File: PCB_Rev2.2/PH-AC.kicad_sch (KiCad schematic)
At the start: 52 parts, among them J1 USB_C_Receptacle_USB2.0_14P, J2 Conn_01x03, Q1 DMG1012T, SW1 SW_Push, U1 RP2040, U2 RT6150B-33GQW, U3 W25Q16JVSS, Y1 Crystal_GND24

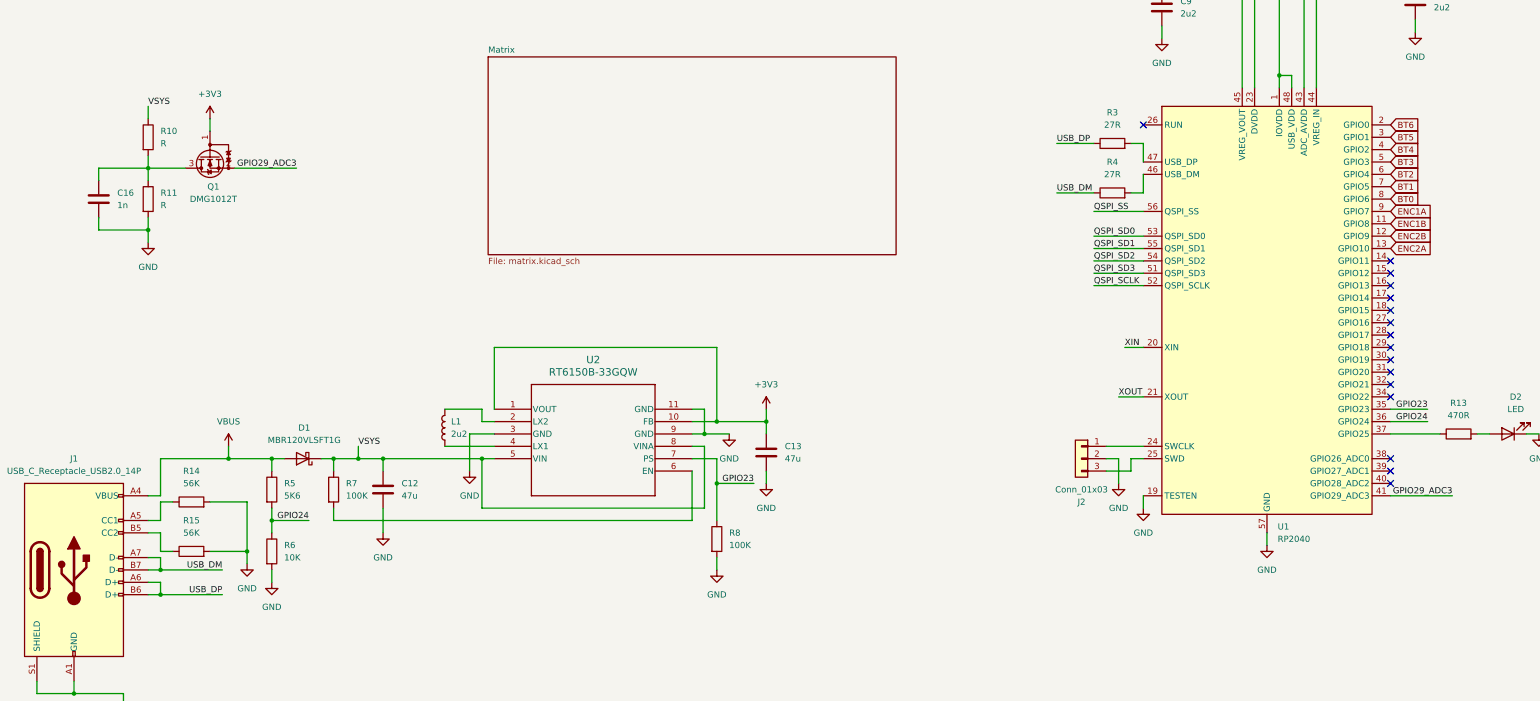
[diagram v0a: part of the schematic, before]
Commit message: LDO Modification
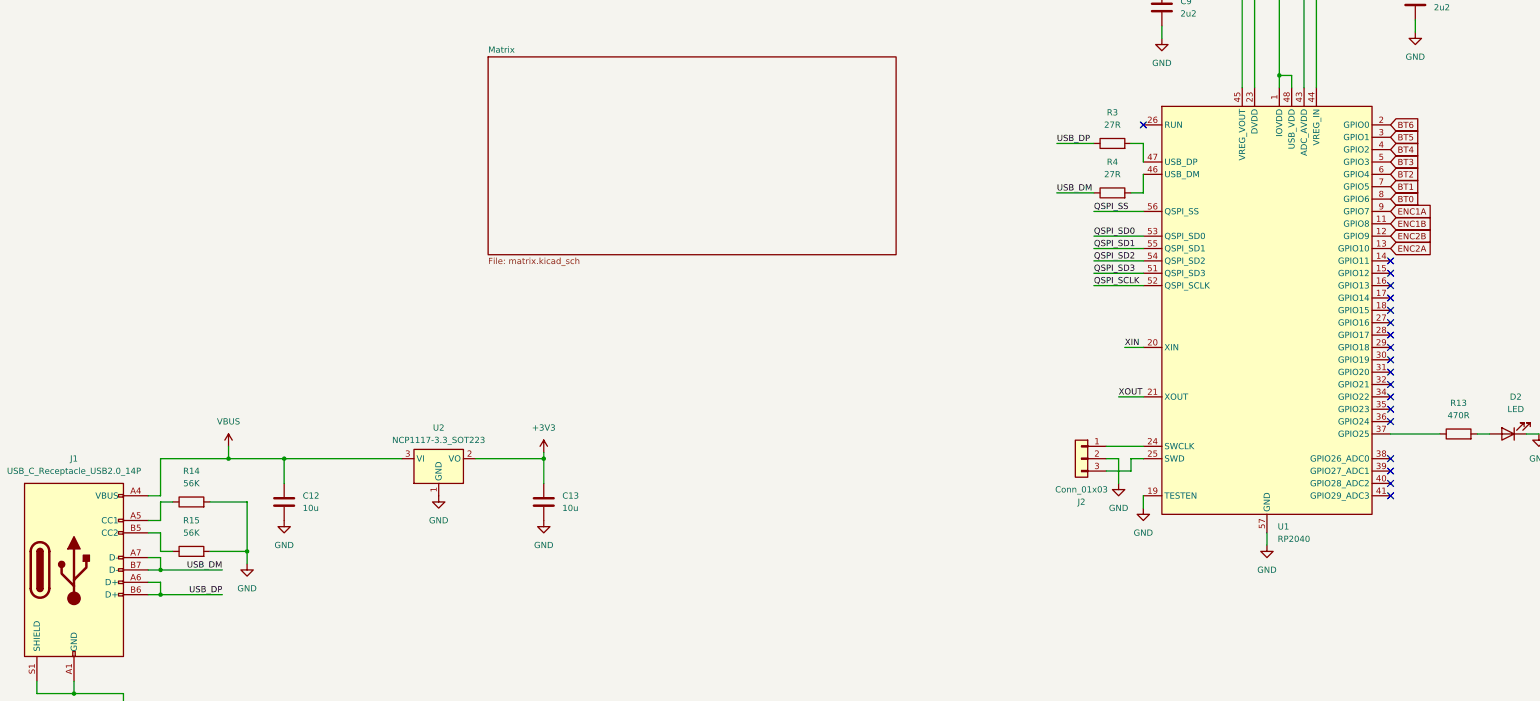
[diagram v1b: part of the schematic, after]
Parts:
- removed C16: 1n, Capacitor_SMD:C_0402_1005Metric, symbol Device:C
- removed D1: MBR120VLSFT1G, Diode_SMD:D_SOD-123F, symbol Device:D_Schottky
- removed L1: 2u2, Capacitor_SMD:C_0402_1005Metric, symbol Device:L
- removed Q1: DMG1012T, Package_TO_SOT_SMD:SOT-523, symbol Transistor_FET:DMG1012T
- removed R10, R11: R, Resistor_SMD:R_0402_1005Metric, symbol Device:R
- removed R5: 5K6, Resistor_SMD:R_0402_1005Metric, symbol Device:R
- removed R6: 10K, Resistor_SMD:R_0402_1005Metric, symbol Device:R
- removed R7, R8: 100K, Resistor_SMD:R_0402_1005Metric, symbol Device:R
- removed U2: RT6150B-33GQW, 10-WFDFN-EP_RIT, symbol 2024-07-21_11-18-28:RT6150B-33GQW
- added U2: NCP1117-3.3_SOT223, Package_TO_SOT_SMD:SOT-223, symbol Regulator_Linear:NCP1117-3.3_SOT223
- C12, C13: value 47u -> 10u; footprint Capacitor_SMD:C_0805_2012Metric -> Capacitor_SMD:C_0402_1005Metric
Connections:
- net VSYS is gone; now on net VBUS: C12.1
- net +3V3: now also U2.2 (VO)
- net GND: now also U2.1 (GND)
- net VBUS: now also U2.3 (VI)
- net GPIO23: no longer names the net of U1.35 (GPIO23)
- net GPIO24: no longer names the net of U1.36 (GPIO24)
- net GPIO29_ADC3: no longer names the net of U1.41 (GPIO29_ADC3)
- no-connect marks 16 -> 19

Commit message: Detail Update
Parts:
- J2: footprint Connector_PinHeader_1.00mm:PinHeader_1x03_P1.00mm_Vertical -> Connector_PinHeader_2.54mm:PinHeader_1x03_P2.54mm_Vertical
- SW1: footprint Connector_PinHeader_1.00mm:PinHeader_1x02_P1.00mm_Vertical -> Button_Switch_THT:SW_PUSH_6mm

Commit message: Changing Footprint
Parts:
- SW1: footprint Button_Switch_THT:SW_PUSH_6mm -> Connector_PinHeader_2.00mm:PinHeader_1x02_P2.00mm_Vertical
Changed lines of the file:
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@@
 			)
 		)
-		(property "Footprint" "Button_Switch_THT:SW_PUSH_6mm"
+		(property "Footprint" "Connector_PinHeader_2.00mm:PinHeader_1x02_P2.00mm_Vertical"
 			(at 59.69 67.31 0)
 			(effects

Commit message: Still Tinkering
Changed the package of 27ohm resistor from 0402 to 0603 to avoid extra expenses

Changed the capacitance of C17 and C18 from 15p to 20p to match the new 12Mhz crystal
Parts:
- C17, C18: value 15p -> 20p
- R14, R15: value 56K -> 5K1
- R3, R4: footprint Resistor_SMD:R_0402_1005Metric -> Resistor_SMD:R_0603_1608Metric
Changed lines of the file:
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@@
 			)
 		)
-		(property "Value" "56K"
+		(property "Value" "5K1"
 			(at 81.28 205.74 90)
 			(effects
@@
 			)
 		)
-		(property "Value" "15p"
+		(property "Value" "20p"
 			(at 177.8 76.1999 0)
 			(effects
@@
 			)
 		)
-		(property "Footprint" "Resistor_SMD:R_0402_1005Metric"
+		(property "Footprint" "Resistor_SMD:R_0603_1608Metric"
 			(at 270.51 137.668 90)
 			(effects
@@
 			)
 		)
-		(property "Value" "15p"
+		(property "Value" "20p"
 			(at 160.02 76.1999 0)
 			(effects
@@
 			)
 		)
-		(property "Value" "56K"
+		(property "Value" "5K1"
 			(at 81.28 215.9 90)
 			(effects
@@
 			)
 		)
-		(property "Footprint" "Resistor_SMD:R_0402_1005Metric"
+		(property "Footprint" "Resistor_SMD:R_0603_1608Metric"
 			(at 270.51 147.828 90)
 			(effects

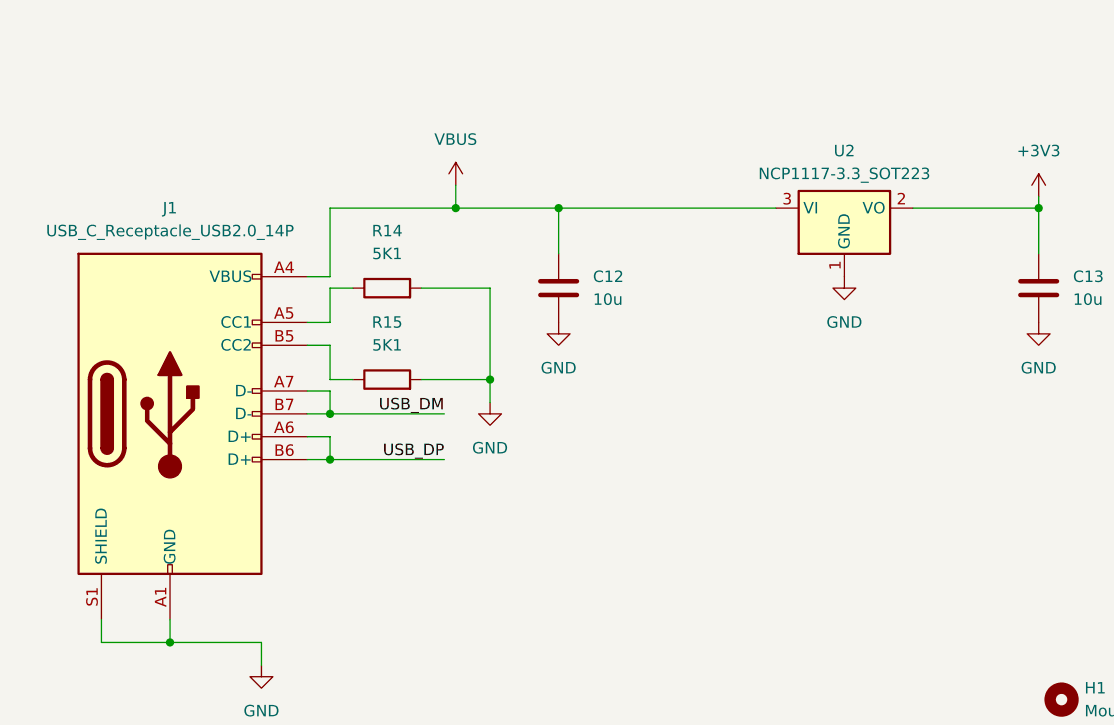
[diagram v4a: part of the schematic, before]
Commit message: LDO Replacement
Changed NCP1117-3.3 to AMS1117-3.3 to avoid extra expenses, again
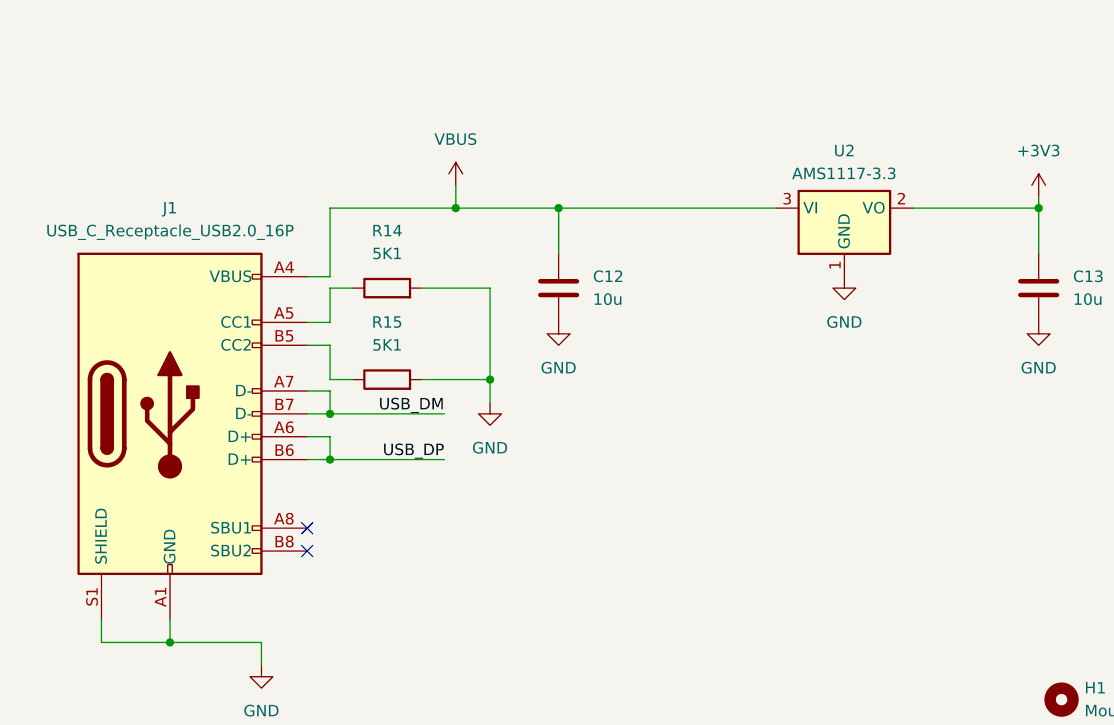
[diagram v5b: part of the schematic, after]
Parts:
- J1: value USB_C_Receptacle_USB2.0_14P -> USB_C_Receptacle_USB2.0_16P; symbol Connector:USB_C_Receptacle_USB2.0_14P -> Connector:USB_C_Receptacle_USB2.0_16P
- U2: value NCP1117-3.3_SOT223 -> AMS1117-3.3; footprint Package_TO_SOT_SMD:SOT-223 -> Package_TO_SOT_SMD:SOT-223-3_TabPin2; symbol Regulator_Linear:NCP1117-3.3_SOT223 -> Regulator_Linear:AMS1117-3.3
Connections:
- no-connect marks 19 -> 21
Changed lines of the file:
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@@
 	)
 	(no_connect
+		(at 72.39 236.22)
+	)
+	(no_connect
+		(at 72.39 238.76)
+	)
+	(no_connect
 		(at 327.66 170.18)
 	)
@@
 	)
 	(symbol
-		(lib_id "Regulator_Linear:NCP1117-3.3_SOT223")
+		(lib_id "Regulator_Linear:AMS1117-3.3")
 		(at 132.08 200.66 0)
 		(unit 1)
@@
 			)
 		)
-		(property "Value" "NCP1117-3.3_SOT223"
+		(property "Value" "AMS1117-3.3"
 			(at 132.08 196.85 0)
 			(effects
@@
 			)
 		)
-		(property "Footprint" "Package_TO_SOT_SMD:SOT-223"
+		(property "Footprint" "Package_TO_SOT_SMD:SOT-223-3_TabPin2"
 			(at 132.08 195.58 0)
 			(effects
@@
 			)
 		)
-		(property "Datasheet" "http://www.onsemi.com/pub_link/Collateral/NCP1117-D.PDF"
+		(property "Datasheet" "http://www.advanced-monolithic.com/pdf/ds1117.pdf"
 			(at 134.62 207.01 0)
 			(effects
@@
 			)
 		)
-		(property "Description" "1A Low drop-out regulator, Fixed Output 3.3V, SOT-223"
+		(property "Description" "1A Low Dropout regulator, positive, 3.3V fixed output, SOT-223"
 			(at 132.08 200.66 0)
 			(effects
@@
 	)
 	(symbol
-		(lib_id "Connector:USB_C_Receptacle_USB2.0_14P")
+		(lib_id "Connector:USB_C_Receptacle_USB2.0_16P")
 		(at 57.15 223.52 0)
 		(unit 1)
@@
 			)
 		)
-		(property "Value" "USB_C_Receptacle_USB2.0_14P"
+		(property "Value" "USB_C_Receptacle_USB2.0_16P"
 			(at 57.15 203.2 0)
 			(effects
@@
 			)
 		)
-		(property "Description" "USB 2.0-only 14P Type-C Receptacle connector"
+		(property "Description" "USB 2.0-only 16P Type-C Receptacle connector"
 			(at 57.15 223.52 0)
 			(effects
@@
 		(pin "A7"
 		)
+		(pin "B8"
+		)
+		(pin "A8"
+		)
 		(instances

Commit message: Redesign
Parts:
- removed C1, C2, C3, C4, C5: 100n, Capacitor_SMD:C_0402_1005Metric, symbol Device:C
- removed D2: LED, LED_SMD:LED_1206_3216Metric, symbol Device:LED
- removed J2: Conn_01x03, Connector_PinHeader_2.54mm:PinHeader_1x03_P2.54mm_Vertical, symbol Connector_Generic:Conn_01x03
- removed R1: 1R, Resistor_SMD:R_0402_1005Metric, symbol Device:R
- removed R13: 470R, Resistor_SMD:R_0402_1005Metric, symbol Device:R
- removed R2: 200R, Resistor_SMD:R_0402_1005Metric, symbol Device:R
- added C12, C13, C15, C16: 100n, Capacitor_SMD:C_0402_1005Metric, symbol Device:C
- C10: value 2u2 -> 1u
- C11, C14, C9: value 2u2 -> 100n
- C8: value 100n -> 1u
- renumbered C12 to C1, C17 to C2, C18 to C3, C13 to C4, C15 to C5, R9 to R1, R12 to R5, R14 to R6, R15 to R7
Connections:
- net +1V1: now also C6.1; no longer C9.1
- net +3V3: now also C11.1, C9.1, U1.43 (ADC_AVDD), C12.1, C13.1, C15.1, C16.1; no longer C6.1
- net GND: now also C12.2, C13.2, C15.2, C16.2
- net USB_DM renamed USB_DN
- no-connect marks 21 -> 24
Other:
- moved on the sheet: C4, C5, U2

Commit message: Revert "Redesign"
This reverts commit 8763a19c73a96b1086359286b52022891444512d.
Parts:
- removed C12, C13, C15, C16: 100n, Capacitor_SMD:C_0402_1005Metric, symbol Device:C
- added C1, C2, C3, C4, C5: 100n, Capacitor_SMD:C_0402_1005Metric, symbol Device:C
- added D2: LED, LED_SMD:LED_1206_3216Metric, symbol Device:LED
- added J2: Conn_01x03, Connector_PinHeader_2.54mm:PinHeader_1x03_P2.54mm_Vertical, symbol Connector_Generic:Conn_01x03
- added R1: 1R, Resistor_SMD:R_0402_1005Metric, symbol Device:R
- added R13: 470R, Resistor_SMD:R_0402_1005Metric, symbol Device:R
- added R2: 200R, Resistor_SMD:R_0402_1005Metric, symbol Device:R
- C10: value 1u -> 2u2
- C11, C14, C9: value 100n -> 2u2
- C8: value 1u -> 100n
- renumbered C1 to C12, C4 to C13, C5 to C15, C2 to C17, C3 to C18, R5 to R12, R6 to R14, R7 to R15, R1 to R9
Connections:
- net +1V1: now also C9.1; no longer C6.1
- net +3V3: now also C6.1, C1.1, C2.1, C3.1, C4.1, C5.1, R2.1; no longer C11.1, C9.1, U1.43 (ADC_AVDD)
- net GND: now also C1.2, C2.2, C3.2, C4.2, C5.2, D2.1 (K), J2.2 (Pin_2)
- net at U1.24 (SWCLK): now also J2.1 (Pin_1)
- net at U1.25 (SWD): now also J2.3 (Pin_3)
- net at U1.37 (GPIO25): now also R13.1
- net USB_DN renamed USB_DM
- new net: R1.1, R2.2
- new net: C11.1, R1.2, U1.43 (ADC_AVDD)
- new net: D2.2 (A), R13.2
- no-connect marks 24 -> 21
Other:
- moved on the sheet: C13, C15, U2

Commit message: Before merge & open source.
Co-Authored-By: MAltmann <57740314+maltmannx@users.noreply.github.com>
Co-Authored-By: nonameCCC <79012391+nonameCCC@users.noreply.github.com>
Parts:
- J2: now left out of the parts list
- JP1: renamed from SW1; value SW_Push -> BOOT_SEL; now left out of the parts list
- U3: value W25Q16JVSS -> W25Q128JVSIQ; symbol Memory_Flash:W25Q16JVSS -> Memory_Flash:W25Q128JVS
- Y1: value Crystal_GND24 -> X322512MSB4SI
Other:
- removed sheet Matrix
- added sheet Switch&Encoder (matrix.kicad_sch)
- note added: "Crystal"
- note added: "Flash"
- note added: "Mounting Hole"
- note added: "RP2040"
- note added: "Switch&Encoder"
- note added: "USB-C&Power"
- company: (none) -> Team PHDesign
- title: (none) -> PH-AC  --Arcade controller for Genshin-impact-like games.
- moved on the sheet: C1, C10, C11, C12, C13, C14, C15, C17, C18, C2, C3, C4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
